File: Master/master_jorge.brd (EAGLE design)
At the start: 42.9 x 34.3 mm, 51 parts, among them J1 ISP, K1 653002114822, K2 653002114822, K3 653002114822, K4 653002114822, U1 ATMEGA128RFA1, U3 ULN2003ADR, Y1 16MHz, Y2 32.768kHz

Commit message: DRC Check changes
Updating master_jorge board with some DRC checks.
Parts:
- moved A1 1.20 mm to (32.5, 32.4)
- moved C18 1.20 mm to (7.34, 16.4)
- moved C1 1.20 mm to (39.3, 27.1)
- moved C11 1.20 mm to (27.9, 27.1)
- moved C12 1.20 mm to (7.34, 9.07)
- moved C14 1.20 mm to (13.4, 11.9)
- moved C16 1.20 mm to (37.1, 27.1)
- moved C19 1.20 mm to (7.34, 18.5)
- moved C2 1.20 mm to (22.3, 27.1)
- moved C20 1.20 mm to (7.34, 20.5)
- moved C21 1.20 mm to (7.34, 22.5)
- moved C22 1.20 mm to (7.34, 24.3)
- moved C3 1.20 mm to (7.34, 11.4)
- moved C6 1.20 mm to (37.6, 13.9)
- moved C7 1.20 mm to (19.8, 27.1)
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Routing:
- net GND: track 233.9 -> 219.2 mm
- net 3.3V: track 121.5 -> 124.1 mm, vias 4 -> 7
- net RX1: track 34.6 -> 33.0 mm
- net PE4: track 20.0 -> 19.3 mm
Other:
- board size 42.9 x 34.3 mm -> 44.7 x 35.8 mm

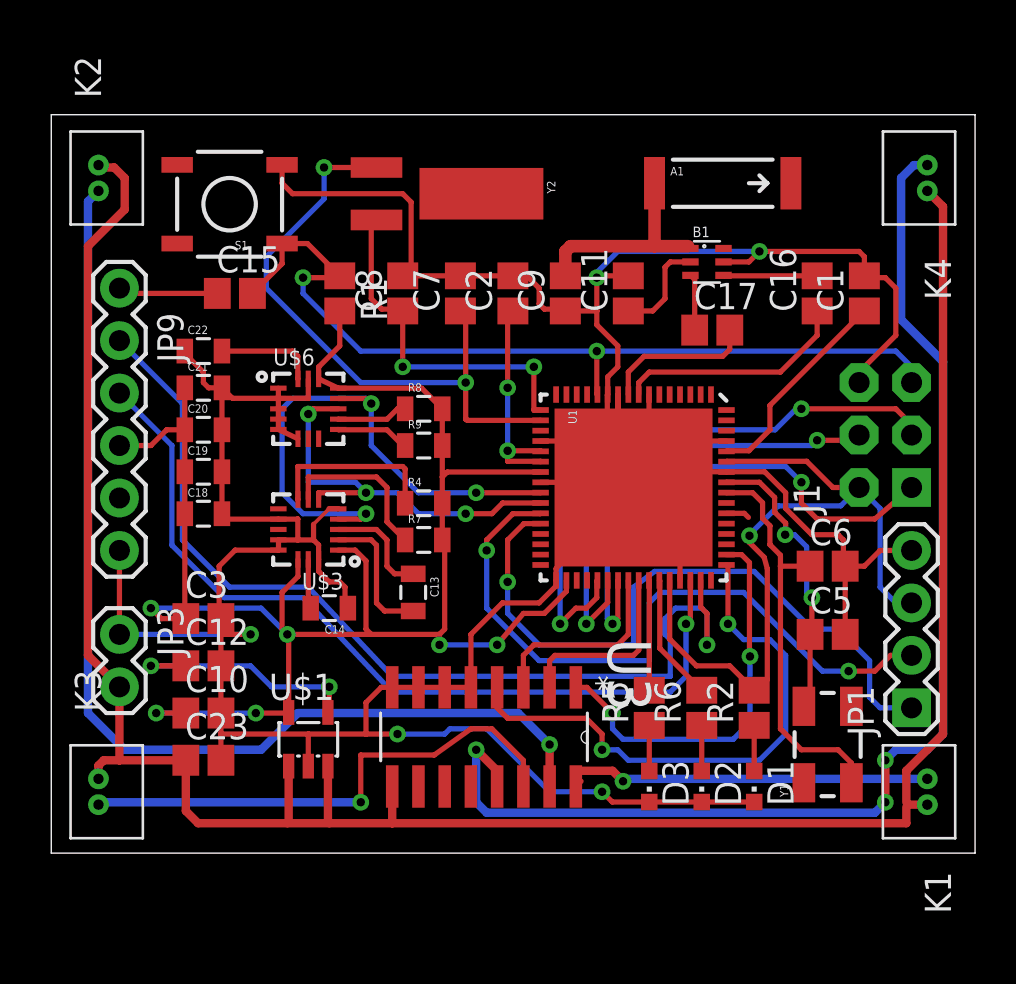
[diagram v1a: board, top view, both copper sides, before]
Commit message: Updating Silkscreen
Updating silkscreen of master_jorge
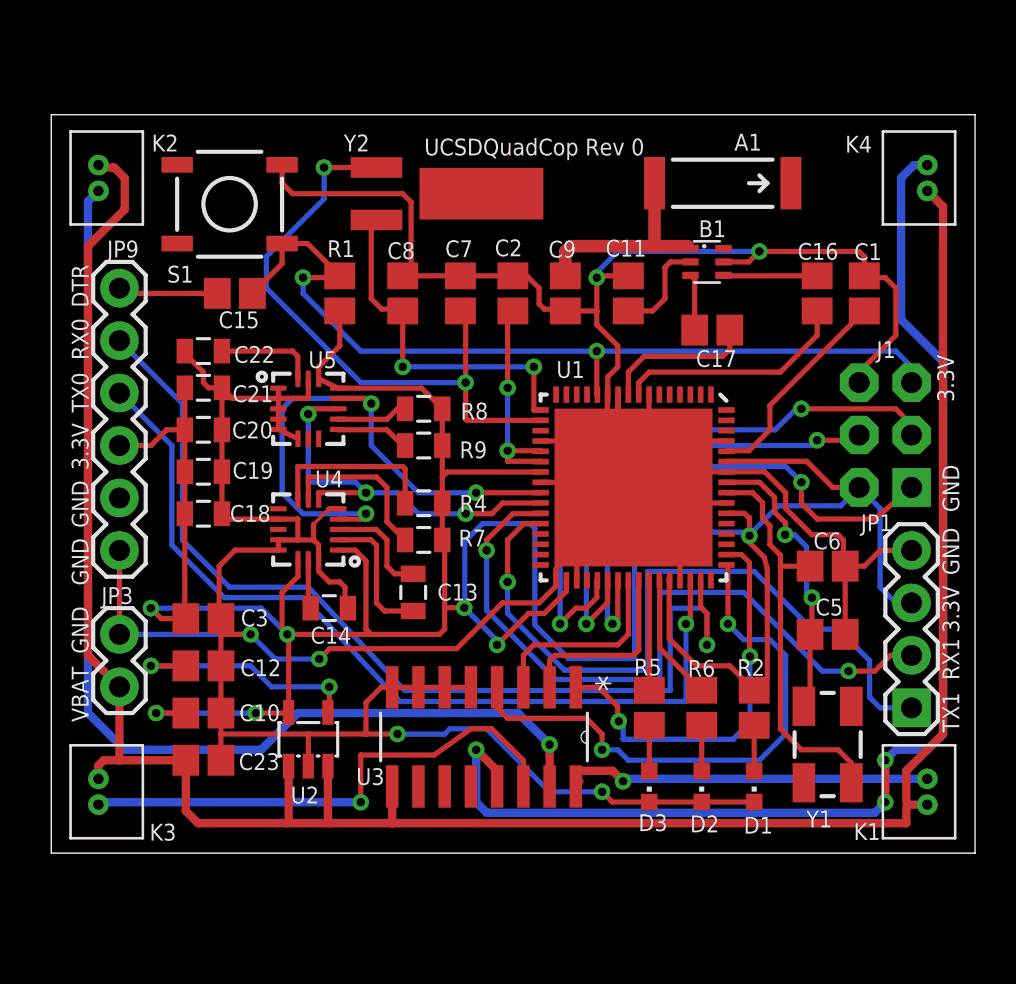
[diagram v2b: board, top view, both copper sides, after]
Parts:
- renumbered U$1 to U2, U$3 to U4, U$6 to U5
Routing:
- net 3.3V: track 124.1 -> 153.3 mm
- net GND: track 219.2 -> 232.3 mm, vias 5 -> 6
- net TX1: track 32.5 -> 34.7 mm
- net RX1: track 33.0 -> 34.6 mm
- net RX0: track 41.4 -> 42.5 mm
- net TX0: track 47.4 -> 48.3 mm
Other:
- board text added: "1.4 inch 35.56 mm"
- board text added: "1.76 inch 44.70 mm"
- board text added: "3.3V"
- board text added: ">Info Board Name: UCSDQuadCop Part Number: 0 Number of Layers: 2 Board Material Type: FR-4 Solder Mask Color: Red Silkscreen Color: White Finish Plating: HASAL Revision Number: 0"
- board text added: "DTR"
- board text added: "GND"
- board text added: "RX0"
- board text added: "RX1"
- board text added: "TX0"
- board text added: "TX1"
- board text added: "UCSDQuadCop Rev 0"
- board text added: "VBAT"
